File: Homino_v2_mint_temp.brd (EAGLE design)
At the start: 27 x 55 mm, 32 parts, among them IC1 LP2950Z, IC2 7805T, Q1 16Mhz

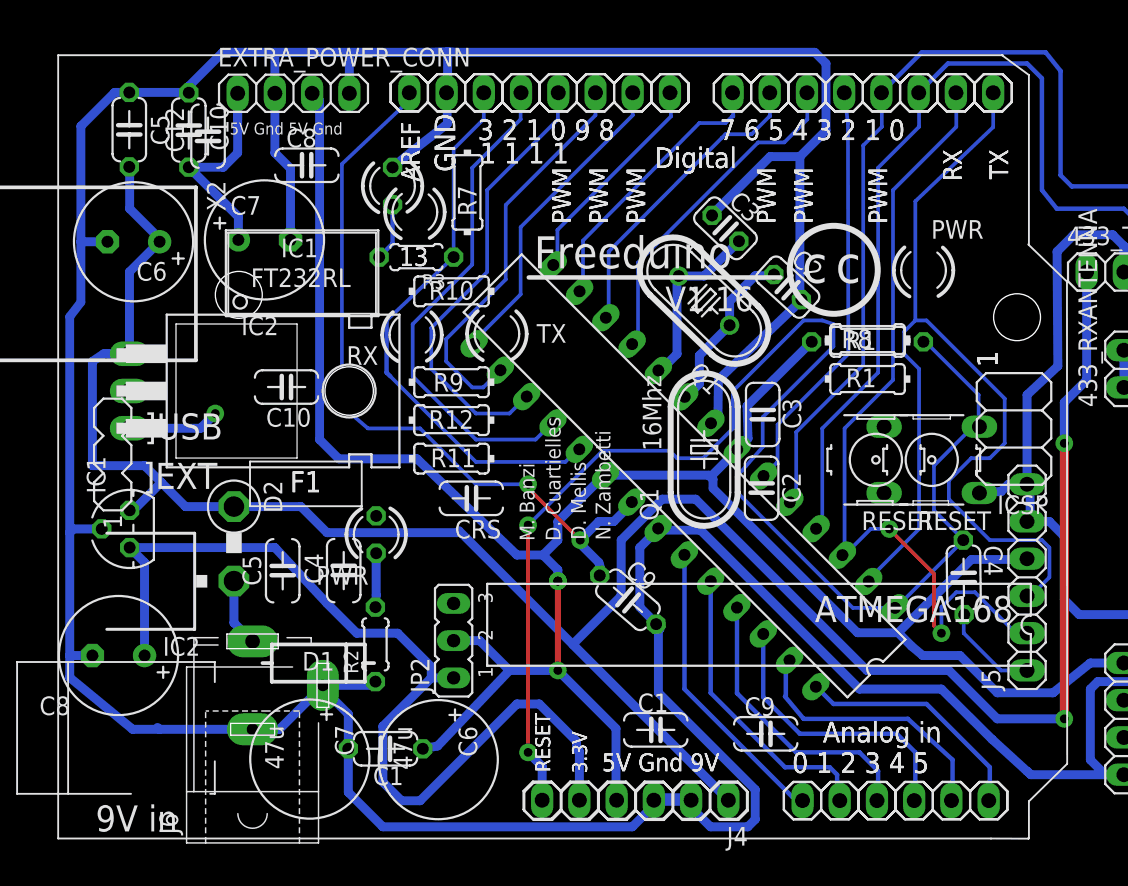
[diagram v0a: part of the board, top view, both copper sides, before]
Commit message: got rid of a jumper on V5.0 line, but maybe there is now a clearance problem with Vin through the voltage selection pin header
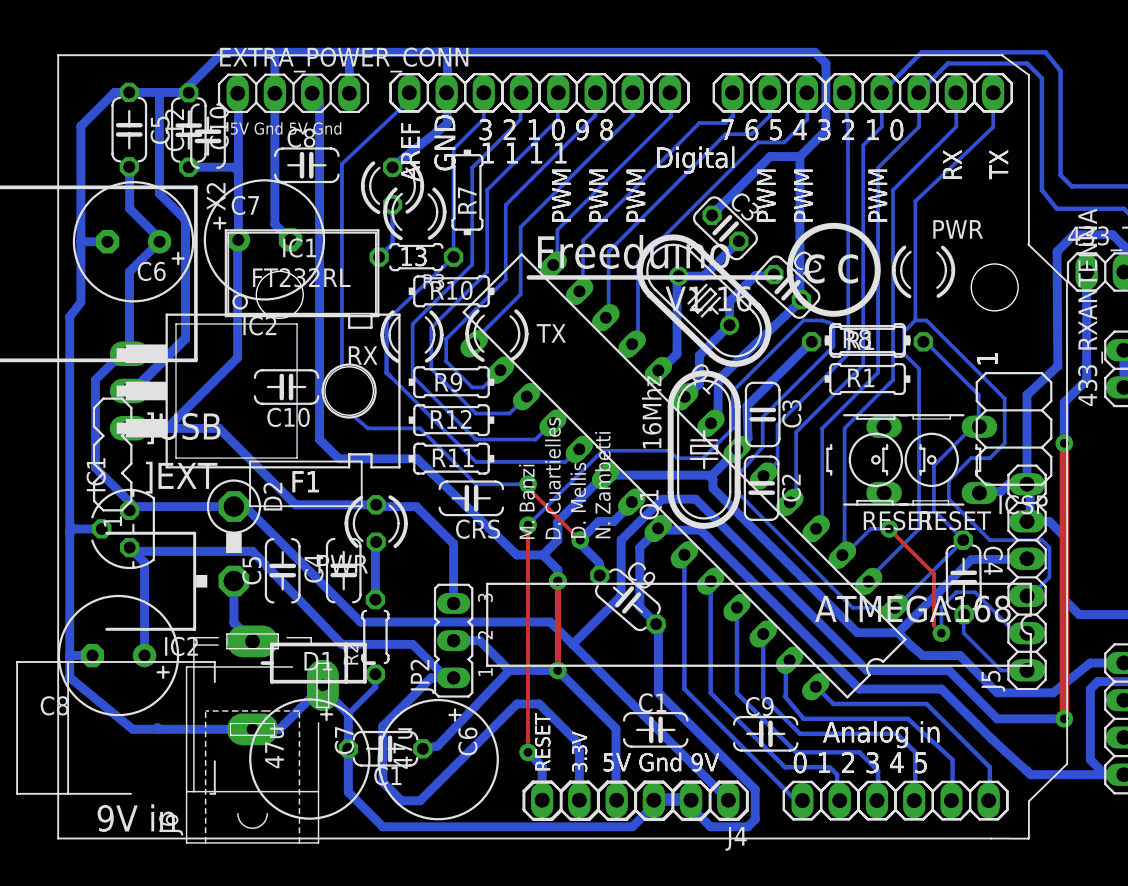
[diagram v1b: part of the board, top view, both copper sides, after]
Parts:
- moved PWR 0.76 mm to (21.6, 21.5)
- moved R2 0.51 mm to (21.6, 13.7)
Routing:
- net V5.0: track 22.2 -> 60.4 mm, vias 1 -> 0
- net GND: track 353.8 -> 381.6 mm
- net VIN: track 173.6 -> 154.2 mm

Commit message: rev.2 of board in beta status
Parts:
- moved C1 17.2 mm to (39.0, 10.2), turned to 45 degrees
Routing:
- net V3.3: track 64.3 -> 47.5 mm
- net DCV: track 150.7 -> 142.6 mm
- net GND: track 381.6 -> 380.7 mm
